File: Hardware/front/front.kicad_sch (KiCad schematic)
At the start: 55 parts, among them J101 Conn_02x10_Odd_Even, SW102 C&K-D6R-Illuminated, SW103 B3W-9002-Y1C, SW104 B3W-9002-Y1C, SW105 B3W-9002-Y1C, SW106 B3W-9002-Y1C, SW107 B3W-9000-RHG2C, U101 XRA1203, U102 AT24CS32-SSHM, U103 PCA9955B, U104 74LV14, U105 74LVC1G14GV

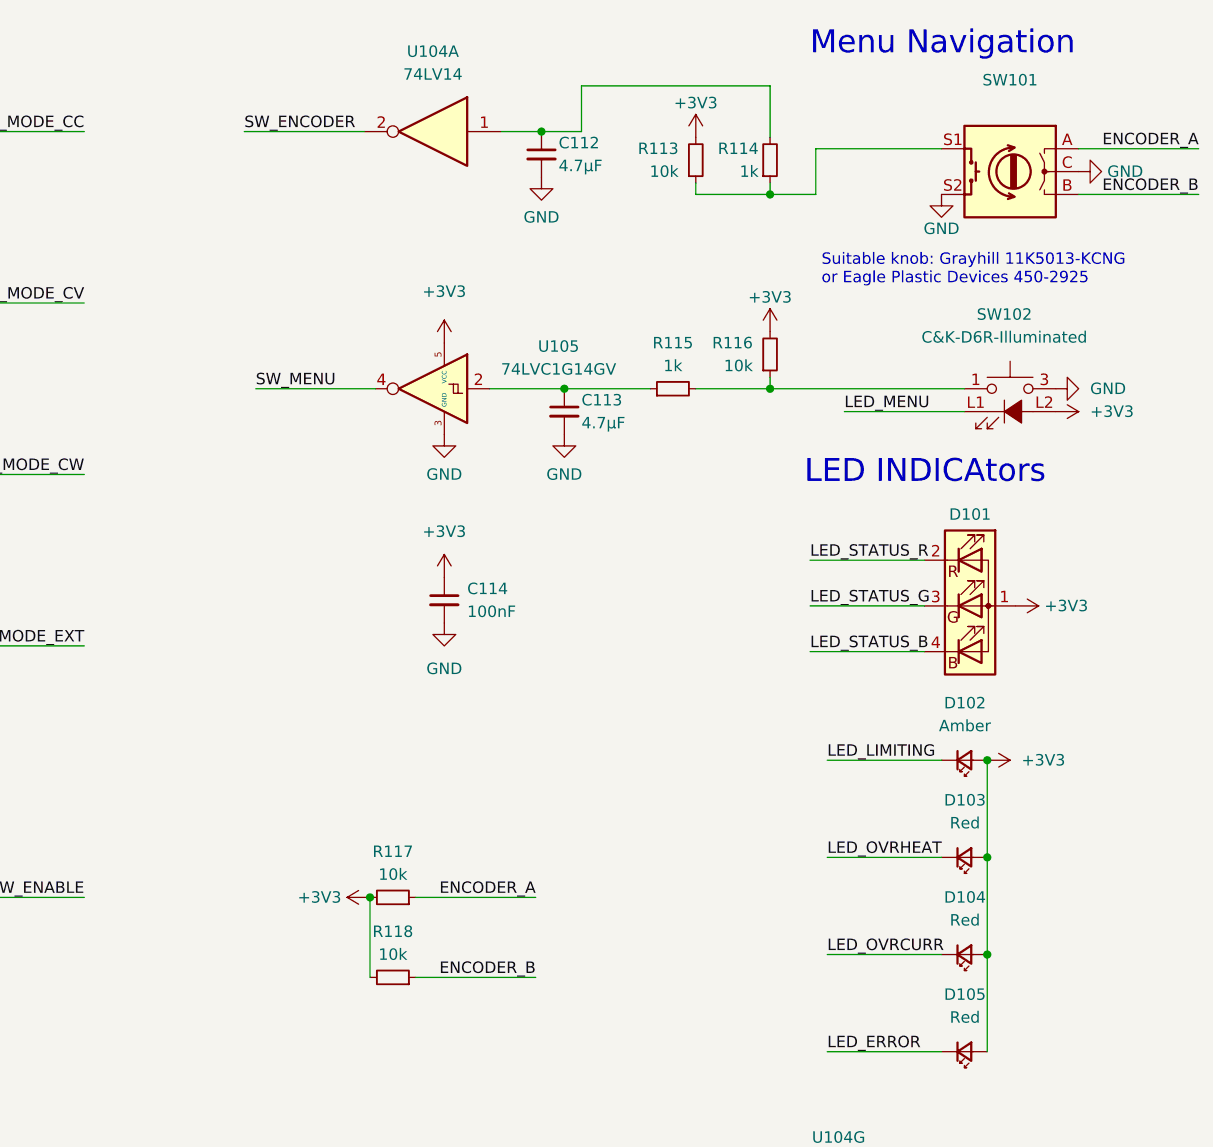
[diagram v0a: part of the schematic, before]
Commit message: Minor tweaks to controller connector layout
- Reduce mechanical interference between load connectors and the bonus
  display mounting studs

- Superficial cleanup of front panel schematic
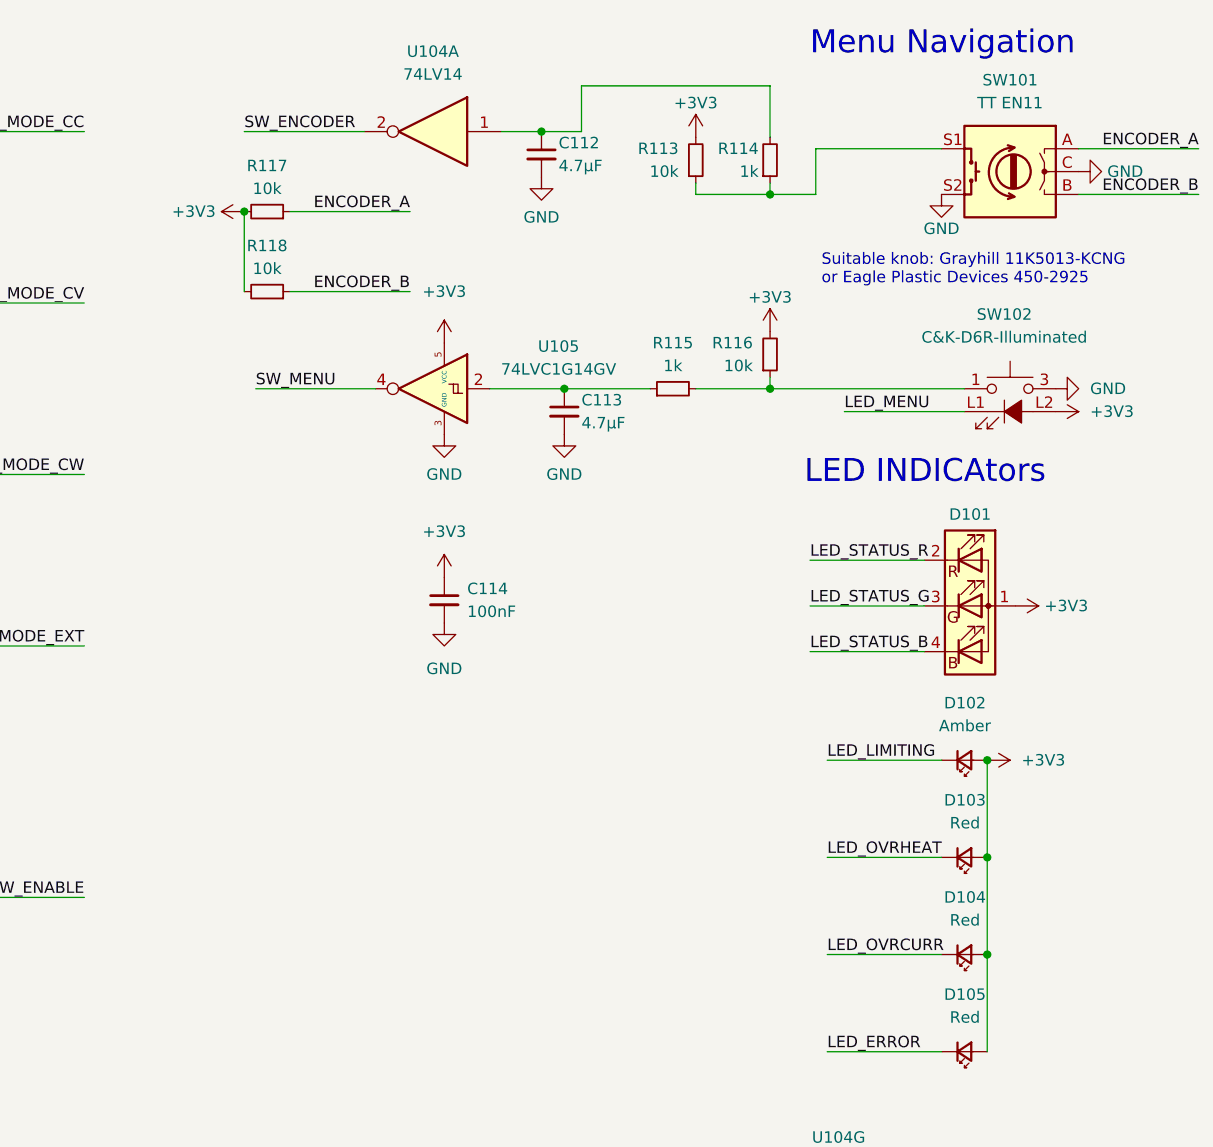
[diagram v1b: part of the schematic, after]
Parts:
- SW101: value (none) -> TT EN11; footprint (none) -> programmable-load:TT_Electronics-EN11-HSM1AF15-0
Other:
- moved on the sheet: R117, R118
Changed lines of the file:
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@@
     (rev "2")
   )
-  (junction (at 189.23 111.125) (diameter 0) (color 0 0 0 0)
+  (junction (at 175.26 34.925) (diameter 0) (color 0 0 0 0)
   )
   (junction (at 97.155 35.56) (diameter 0) (color 0 0 0 0)
@@
     (stroke (width 0) (type default) (color 0 0 0 0))
   )
-  (wire (pts (xy 207.645 111.125) (xy 194.31 111.125))
+  (wire (pts (xy 193.675 34.925) (xy 180.34 34.925))
     (stroke (width 0) (type default) (color 0 0 0 0))
   )
@@
     (stroke (width 0) (type default) (color 0 0 0 0))
   )
-  (wire (pts (xy 189.23 111.125) (xy 189.23 120.015))
+  (wire (pts (xy 175.26 34.925) (xy 175.26 43.815))
     (stroke (width 0) (type default) (color 0 0 0 0))
   )
@@
     (stroke (width 0) (type default) (color 0 0 0 0))
   )
-  (wire (pts (xy 207.645 120.015) (xy 194.31 120.015))
+  (wire (pts (xy 193.675 43.815) (xy 180.34 43.815))
     (stroke (width 0) (type default) (color 0 0 0 0))
   )
@@
     (effects (font (size 1.27 1.27)) (justify right bottom))
   )
-  (label "ENCODER_A" (at 207.645 111.125 180)
+  (label "ENCODER_A" (at 193.675 34.925 180)
     (effects (font (size 1.27 1.27)) (justify right bottom))
   )
@@
     (effects (font (size 1.27 1.27)) (justify left bottom))
   )
-  (label "ENCODER_B" (at 207.645 120.015 180)
+  (label "ENCODER_B" (at 193.675 43.815 180)
     (effects (font (size 1.27 1.27)) (justify right bottom))
   )
@@
     (pin "1")
   )
-  (symbol (lib_id "power:+3V3") (at 189.23 111.125 90) (unit 1)
-    (in_bom yes) (on_board yes) (fields_autoplaced)
-    (property "Reference" "#PWR0150" (id 0) (at 193.04 111.125 0)
-      (effects (font (size 1.27 1.27)) hide)
-    )
-    (property "Value" "+3V3" (id 1) (at 186.055 111.1249 90)
-      (effects (font (size 1.27 1.27)) (justify left))
-    )
-    (property "Footprint" "" (id 2) (at 189.23 111.125 0)
-      (effects (font (size 1.27 1.27)) hide)
-    )
-    (property "Datasheet" "" (id 3) (at 189.23 111.125 0)
+  (symbol (lib_id "power:+3V3") (at 175.26 34.925 90) (unit 1)
+    (in_bom yes) (on_board yes) (fields_autoplaced)
+    (property "Reference" "#PWR0150" (id 0) (at 179.07 34.925 0)
+      (effects (font (size 1.27 1.27)) hide)
+    )
+    (property "Value" "+3V3" (id 1) (at 172.085 34.9249 90)
+      (effects (font (size 1.27 1.27)) (justify left))
+    )
+    (property "Footprint" "" (id 2) (at 175.26 34.925 0)
+      (effects (font (size 1.27 1.27)) hide)
+    )
+    (property "Datasheet" "" (id 3) (at 175.26 34.925 0)
       (effects (font (size 1.27 1.27)) hide)
     )
@@
     (pin "2")
   )
-  (symbol (lib_id "Device:R_Small") (at 191.77 120.015 270) (mirror x) (unit 1)
-    (in_bom yes) (on_board yes)
-    (property "Reference" "R118" (id 0) (at 191.77 114.935 90))
-    (property "Value" "10k" (id 1) (at 191.77 117.475 90))
-    (property "Footprint" "Resistor_SMD:R_0805_2012Metric_Pad1.20x1.40mm_HandSolder" (id 2) (at 191.77 120.015 0)
-      (effects (font (size 1.27 1.27)) hide)
-    )
-    (property "Datasheet" "~" (id 3) (at 191.77 120.015 0)
-      (effects (font (size 1.27 1.27)) hide)
-    )
-    (property "MPN" "RMC1/10-103JTP" (id 4) (at 191.77 120.015 90)
+  (symbol (lib_id "Device:R_Small") (at 177.8 43.815 270) (mirror x) (unit 1)
+    (in_bom yes) (on_board yes)
+    (property "Reference" "R118" (id 0) (at 177.8 38.735 90))
+    (property "Value" "10k" (id 1) (at 177.8 41.275 90))
+    (property "Footprint" "Resistor_SMD:R_0805_2012Metric_Pad1.20x1.40mm_HandSolder" (id 2) (at 177.8 43.815 0)
+      (effects (font (size 1.27 1.27)) hide)
+    )
+    (property "Datasheet" "~" (id 3) (at 177.8 43.815 0)
+      (effects (font (size 1.27 1.27)) hide)
+    )
+    (property "MPN" "RMC1/10-103JTP" (id 4) (at 177.8 43.815 90)
       (effects (font (size 1.27 1.27)) hide)
     )
@@
     (in_bom yes) (on_board yes) (fields_autoplaced)
     (property "Reference" "SW101" (id 0) (at 260.35 20.32 0))
-    (property "Value" "" (id 1) (at 260.35 22.86 0))
-    (property "Footprint" "" (id 2) (at 264.16 26.416 0)
+    (property "Value" "TT EN11" (id 1) (at 260.35 22.86 0))
+    (property "Footprint" "programmable-load:TT_Electronics-EN11-HSM1AF15-0" (id 2) (at 264.16 26.416 0)
       (effects (font (size 1.27 1.27)) hide)
     )
@@
     (pin "2")
   )
-  (symbol (lib_id "Device:R_Small") (at 191.77 111.125 270) (mirror x) (unit 1)
-    (in_bom yes) (on_board yes)
-    (property "Reference" "R117" (id 0) (at 191.77 106.045 90))
-    (property "Value" "10k" (id 1) (at 191.77 108.585 90))
-    (property "Footprint" "Resistor_SMD:R_0805_2012Metric_Pad1.20x1.40mm_HandSolder" (id 2) (at 191.77 111.125 0)
-      (effects (font (size 1.27 1.27)) hide)
-    )
-    (property "Datasheet" "~" (id 3) (at 191.77 111.125 0)
-      (effects (font (size 1.27 1.27)) hide)
-    )
-    (property "MPN" "RMC1/10-103JTP" (id 4) (at 191.77 111.125 90)
-      (effects (font (size 1.27 1.27)) hide)
-    )
+  (symbol (lib_id "Device:R_Small") (at 177.8 34.925 270) (mirror x) (unit 1)
+    (in_bom yes) (on_board yes)
+    (property "Reference" "R117" (id 0) (at 177.8 29.845 90))
+    (property "Value" "10k" (id 1) (at 177.8 32.385 90))
+    (property "Footprint" "Resistor_SMD:R_0805_2012Metric_Pad1.20x1.40mm_HandSolder" (id 2) (at 177.8 34.925 0)
+      (effects (font (size 1.27 1.27)) hide)
+    )
+    (property "Datasheet" "~" (id 3) (at 177.8 34.925 0)
+      (effects (font (size 1.27 1.27)) hide)
+    )
+    (property "MPN" "RMC1/10-103JTP" (id 4) (at 177.8 34.925 90)
+      (effects (font (size 1.27 1.27)) hide)
+    )

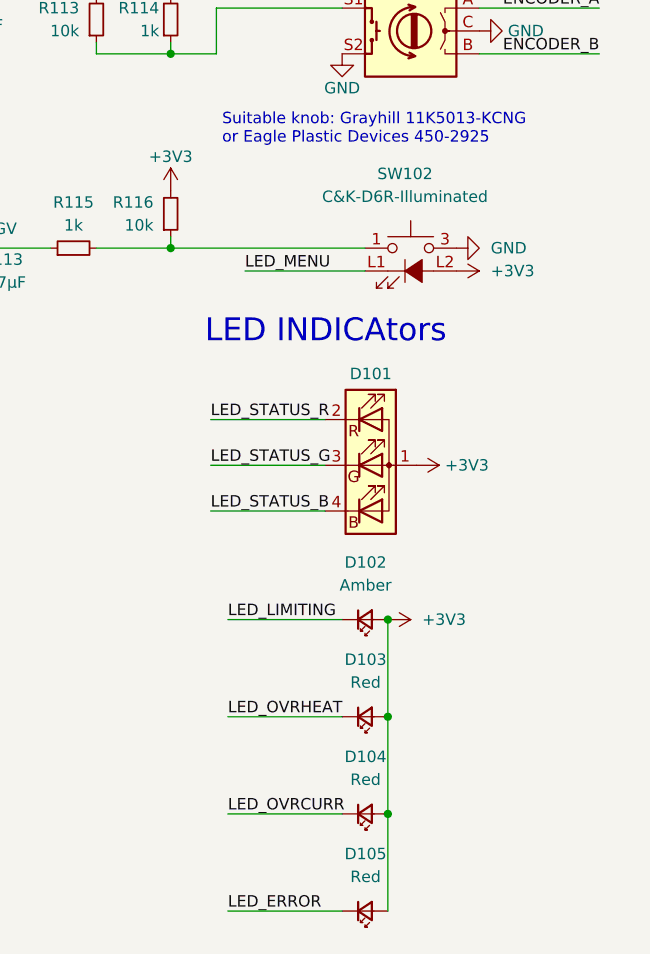
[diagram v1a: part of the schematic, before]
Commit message: Replace menu button on front panel
- Switched the menu button for the same Omron B3W-9xxx type as the rest
  of the switches so it doesn't protrude from the front panel as much
  anymore
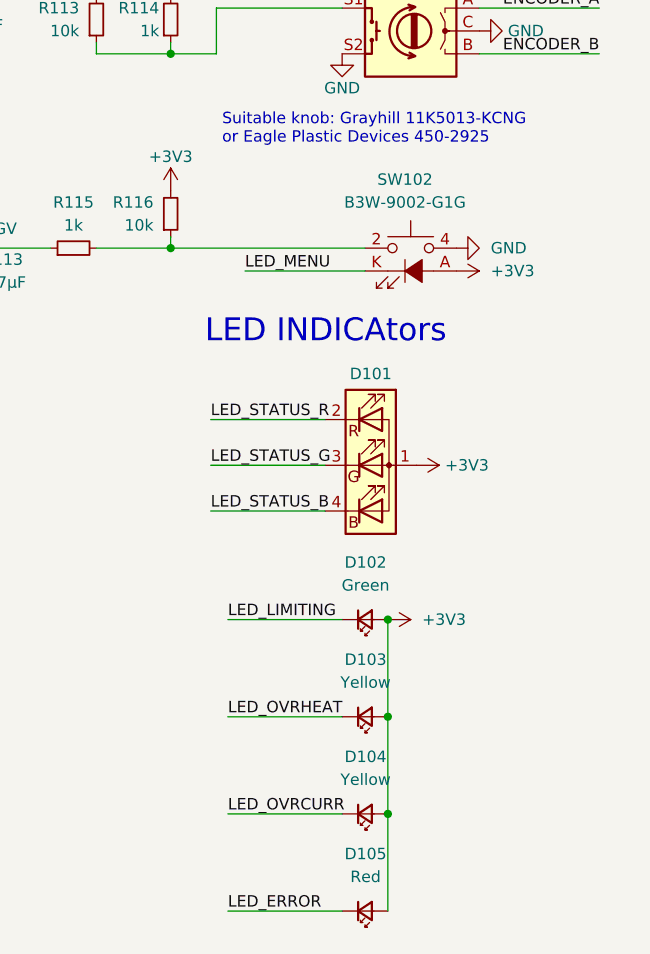
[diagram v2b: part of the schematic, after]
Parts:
- removed SW102: C&K-D6R-Illuminated, programmable-load:C&K-D6R-LED, symbol programmable-load:C&K-D6R-Illuminated
- added SW102: B3W-9002-G1G, programmable-load:Omron-B3W-90XX-X1X, symbol programmable-load:B3W-900X-X1X
- D102: value Amber -> Green; MPN 156120AS82500 -> 156120VS82500
- D103, D104: value Red -> Yellow; MPN 156120RS82500 -> 156120YS82500
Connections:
- net +3V3: now also SW102.A
- net GND: now also SW102.3, SW102.4
- net LED_MENU: now also SW102.K
- net at R115.2, R116.1: now also SW102.1, SW102.2
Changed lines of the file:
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@@
     (pin "2")
+  )
+  (symbol (lib_id "programmable-load:B3W-900X-X1X") (at 260.35 57.15 0) (unit 1)
+    (in_bom yes) (on_board yes)
+    (property "Reference" "SW102" (id 0) (at 259.715 46.99 0))
+    (property "Value" "B3W-9002-G1G" (id 1) (at 259.715 49.53 0))
+    (property "Footprint" "programmable-load:Omron-B3W-90XX-X1X" (id 2) (at 260.35 49.53 0)
+      (effects (font (size 1.27 1.27)) hide)
+    )
+    (property "Datasheet" "https://www.mouser.com/datasheet/2/307/en-b3w-9-11824.pdf" (id 3) (at 260.35 49.53 0)
+      (effects (font (size 1.27 1.27)) hide)
+    )
+    (property "MPN" "B3W-9002-G1G" (id 4) (at 260.35 57.15 0)
+      (effects (font (size 1.27 1.27)) hide)
+    )
+    (pin "1")
+    (pin "2")
+    (pin "3")
+    (pin "4")
+    (pin "A")
+    (pin "K")
   )
   (symbol (lib_id "power:+3V3") (at 88.9 86.36 0) (unit 1)
@@
     (in_bom yes) (on_board yes) (fields_autoplaced)
     (property "Reference" "D102" (id 0) (at 255.3335 89.535 0))
-    (property "Value" "Amber" (id 1) (at 255.3335 92.075 0))
+    (property "Value" "Green" (id 1) (at 255.3335 92.075 0))
     (property "Footprint" "LED_SMD:LED_1206_3216Metric_Pad1.42x1.75mm_HandSolder" (id 2) (at 255.27 95.885 90)
       (effects (font (size 1.27 1.27)) hide)
@@
       (effects (font (size 1.27 1.27)) hide)
     )
-    (property "MPN" "156120AS82500" (id 4) (at 255.27 95.885 0)
+    (property "MPN" "156120VS82500" (id 4) (at 255.27 95.885 0)
       (effects (font (size 1.27 1.27)) hide)
     )
@@
     (in_bom yes) (on_board yes) (fields_autoplaced)
     (property "Reference" "D104" (id 0) (at 255.3335 111.125 0))
-    (property "Value" "Red" (id 1) (at 255.3335 113.665 0))
+    (property "Value" "Yellow" (id 1) (at 255.3335 113.665 0))
     (property "Footprint" "LED_SMD:LED_1206_3216Metric_Pad1.42x1.75mm_HandSolder" (id 2) (at 255.27 117.475 90)
       (effects (font (size 1.27 1.27)) hide)
@@
       (effects (font (size 1.27 1.27)) hide)
     )
-    (property "MPN" "156120RS82500" (id 4) (at 255.27 117.475 0)
+    (property "MPN" "156120YS82500" (id 4) (at 255.27 117.475 0)
       (effects (font (size 1.27 1.27)) hide)
     )
@@
     (pin "1")
     (pin "2")
-  )
-  (symbol (lib_id "programmable-load:C&K-D6R-Illuminated") (at 260.35 50.8 0) (unit 1)
-    (in_bom yes) (on_board yes) (fields_autoplaced)
-    (property "Reference" "SW102" (id 0) (at 259.715 46.355 0))
-    (property "Value" "C&K-D6R-Illuminated" (id 1) (at 259.715 48.895 0))
-    (property "Footprint" "programmable-load:C&K-D6R-LED" (id 2) (at 260.35 50.8 0)
-      (effects (font (size 1.27 1.27)) hide)
-    )
-    (property "Datasheet" "https://www.mouser.com/datasheet/2/60/d6-1382571.pdf" (id 3) (at 260.35 50.8 0)
-      (effects (font (size 1.27 1.27)) hide)
-    )
-    (property "MPN" "D6RLRD F1 LFS" (id 4) (at 260.35 50.8 0)
-      (effects (font (size 1.27 1.27)) hide)
-    )
-    (pin "1")
-    (pin "2")
-    (pin "3")
-    (pin "4")
-    (pin "L1")
-    (pin "L2")
   )
   (symbol (lib_id "power:GND") (at 252.73 33.02 0) (mirror y) (unit 1)
@@
     (in_bom yes) (on_board yes) (fields_autoplaced)
     (property "Reference" "D103" (id 0) (at 255.3335 100.33 0))
-    (property "Value" "Red" (id 1) (at 255.3335 102.87 0))
+    (property "Value" "Yellow" (id 1) (at 255.3335 102.87 0))
     (property "Footprint" "LED_SMD:LED_1206_3216Metric_Pad1.42x1.75mm_HandSolder" (id 2) (at 255.27 106.68 90)
       (effects (font (size 1.27 1.27)) hide)
@@
       (effects (font (size 1.27 1.27)) hide)
     )
-    (property "MPN" "156120RS82500" (id 4) (at 255.27 106.68 0)
+    (property "MPN" "156120YS82500" (id 4) (at 255.27 106.68 0)
       (effects (font (size 1.27 1.27)) hide)
     )
@@
     )
     (path "/aa5002d5-4826-4046-ad75-e5fc5f089abf"
-      (reference "D102") (unit 1) (value "Amber") (footprint "LED_SMD:LED_1206_3216Metric_Pad1.42x1.75mm_HandSolder")
+      (reference "D102") (unit 1) (value "Green") (footprint "LED_SMD:LED_1206_3216Metric_Pad1.42x1.75mm_HandSolder")
     )
     (path "/e3e4603c-dc13-4d5d-a413-87cd8b770541"
-      (reference "D103") (unit 1) (value "Red") (footprint "LED_SMD:LED_1206_3216Metric_Pad1.42x1.75mm_HandSolder")
+      (reference "D103") (unit 1) (value "Yellow") (footprint "LED_SMD:LED_1206_3216Metric_Pad1.42x1.75mm_HandSolder")
     )
     (path "/aaedccfd-6066-41db-bd95-6515e1d03b58"
-      (reference "D104") (unit 1) (value "Red") (footprint "LED_SMD:LED_1206_3216Metric_Pad1.42x1.75mm_HandSolder")
+      (reference "D104") (unit 1) (value "Yellow") (footprint "LED_SMD:LED_1206_3216Metric_Pad1.42x1.75mm_HandSolder")
     )
     (path "/ef96cc2a-22a5-4afc-ba03-9df1ce9a8d1b"
@@
       (reference "SW101") (unit 1) (value "TT EN11") (footprint "programmable-load:TT_Electronics-EN11-HSM1AF15-0")
     )
-    (path "/c748ca36-6c04-4ba0-a4b6-196d9bddcb36"
-      (reference "SW102") (unit 1) (value "C&K-D6R-Illuminated") (footprint "programmable-load:C&K-D6R-LED")
+    (path "/589178f6-2f4a-44bd-967d-3cc7cd491f6c"
+      (reference "SW102") (unit 1) (value "B3W-9002-G1G") (footprint "programmable-load:Omron-B3W-90XX-X1X")
     )
     (path "/0b6e29ac-6305-4036-ae93-0b6173488c86"
